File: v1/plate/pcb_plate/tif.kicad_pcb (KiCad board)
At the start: 2 copper layers, 161.7 x 126 mm, 33 parts, among them J2 MJ-4PP-9, SW24 SW_PUSH, SW24B1 SW_PUSH, SW25 SW_PUSH, SW25B1 SW_PUSH, SW26 SW_PUSH, SW26B1 SW_PUSH, U1 ProMicro

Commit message: hole for rotary encoder
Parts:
- removed D23: D, SofleKeyboard-footprint:Diode_SOD123
- removed ROT_ENC: Rotary_Encoder_Switch, SofleKeyboard-footprint:RotaryEncoder_Alps_EC11E-Switch_Vertical_H20mm-keebio_modified
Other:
- outline, holes or cut-outs redrawn
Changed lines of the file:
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@@
   (general
     (thickness 1.6)
-    (drawings 121)
+    (drawings 124)
     (tracks 956)
     (zones 0)
-    (modules 33)
+    (modules 31)
     (nets 54)
   )
@@
       (net 28 "Net-(D24-Pad2)"))
   )
-  (module SofleKeyboard-footprint:RotaryEncoder_Alps_EC11E-Switch_Vertical_H20mm-keebio_modified (layer F.Cu)
-    (at 163.0299 126.2126 180)
-    (descr "Alps rotary encoder, EC12E... with switch, vertical shaft, http://www.alps.com/prod/info/E/HTML/Encoder/Incremental/EC11/EC11E15204A3.html")
-    (tags "rotary encoder")
-    (fp_text reference ROT_ENC (at -0.0127 8.3693) (layer F.SilkS)
-      (effects (font (size 1 1) (thickness 0.15)))
-    )
-    (fp_text value Rotary_Encoder_Switch (at 0 7.9) (layer F.Fab)
-      (effects (font (size 1 1) (thickness 0.15)))
-    )
-    (fp_line (start -0.5 0) (end 0.5 0) (layer B.SilkS) (width 0.12))
-    (fp_line (start 0 -0.5) (end 0 0.5) (layer B.SilkS) (width 0.12))
-    (fp_circle (center 0 0) (end 3 0) (layer B.SilkS) (width 0.12))
-    (fp_line (start 2 -5.9) (end 6.1 -5.9) (layer B.SilkS) (width 0.12))
-    (fp_line (start 6.1 -5.9) (end 6.1 -3.5) (layer B.SilkS) (width 0.12))
-    (fp_line (start 6.1 -1.3) (end 6.1 1.3) (layer B.SilkS) (width 0.12))
-    (fp_line (start 6.1 3.5) (end 6.1 5.9) (layer B.SilkS) (width 0.12))
-    (fp_line (start 6.1 5.9) (end 2 5.9) (layer B.SilkS) (width 0.12))
-    (fp_line (start -2 5.9) (end -6.1 5.9) (layer B.SilkS) (width 0.12))
-    (fp_line (start -6.1 -5.9) (end -6.1 5.9) (layer B.SilkS) (width 0.12))
-    (fp_line (start -2 -5.9) (end -6.1 -5.9) (layer B.SilkS) (width 0.12))
-    (fp_line (start -0.5 0) (end 0.5 0) (layer F.SilkS) (width 0.12))
-    (fp_line (start 0 -0.5) (end 0 0.5) (layer F.SilkS) (width 0.12))
-    (fp_line (start 6.1 3.5) (end 6.1 5.9) (layer F.SilkS) (width 0.12))
-    (fp_line (start 6.1 -1.3) (end 6.1 1.3) (layer F.SilkS) (width 0.12))
-    (fp_line (start 6.1 -5.9) (end 6.1 -3.5) (layer F.SilkS) (width 0.12))
-    (fp_line (start -3 0) (end 3 0) (layer F.Fab) (width 0.12))
-    (fp_line (start 0 -3) (end 0 3) (layer F.Fab) (width 0.12))
-    (fp_line (start -6.1 -5.9) (end -6.1 5.9) (layer F.SilkS) (width 0.12))
-    (fp_line (start -2 -5.9) (end -6.1 -5.9) (layer F.SilkS) (width 0.12))
-    (fp_line (start -2 5.9) (end -6.1 5.9) (layer F.SilkS) (width 0.12))
-    (fp_line (start 6.1 5.9) (end 2 5.9) (layer F.SilkS) (width 0.12))
-    (fp_line (start 2 -5.9) (end 6.1 -5.9) (layer F.SilkS) (width 0.12))
-    (fp_line (start -6 -4.7) (end -5 -5.8) (layer F.Fab) (width 0.12))
-    (fp_line (start -6 5.8) (end -6 -4.7) (layer F.Fab) (width 0.12))
-    (fp_line (start 6 5.8) (end -6 5.8) (layer F.Fab) (width 0.12))
-    (fp_line (start 6 -5.8) (end 6 5.8) (layer F.Fab) (width 0.12))
-    (fp_line (start -5 -5.8) (end 6 -5.8) (layer F.Fab) (width 0.12))
-    (fp_line (start -9 -7.1) (end 8.5 -7.1) (layer F.CrtYd) (width 0.05))
-    (fp_line (start -9 -7.1) (end -9 7.1) (layer F.CrtYd) (width 0.05))
-    (fp_line (start 8.5 7.1) (end 8.5 -7.1) (layer F.CrtYd) (width 0.05))
-    (fp_line (start 8.5 7.1) (end -9 7.1) (layer F.CrtYd) (width 0.05))
-    (fp_circle (center 0 0) (end 3 0) (layer F.SilkS) (width 0.12))
-    (fp_circle (center 0 0) (end 3 0) (layer F.Fab) (width 0.12))
-    (pad S1 thru_hole circle (at 7 2.5 180) (size 2 2) (drill 1) (layers *.Cu *.Mask)
-      (net 46 COL2))
-    (pad S2 thru_hole circle (at 7 -2.5 180) (size 2 2) (drill 1) (layers *.Cu *.Mask)
-      (net 52 SW23B))
-    (pad MP thru_hole rect (at 0 5.6 180) (size 3.2 2) (drill oval 2.8 1.5) (layers *.Cu *.Mask))
-    (pad MP thru_hole rect (at 0 -5.6 180) (size 3.2 2) (drill oval 2.8 1.5) (layers *.Cu *.Mask))
-    (pad B thru_hole circle (at -7.5 2.5 180) (size 2 2) (drill 1) (layers *.Cu *.Mask)
-      (net 40 ENCB))
-    (pad C thru_hole circle (at -7.5 0 180) (size 2 2) (drill 1) (layers *.Cu *.Mask)
-      (net 34 GND))
-    (pad A thru_hole circle (at -7.5 -2.5 180) (size 2 2) (drill 1) (layers *.Cu *.Mask)
-      (net 41 ENCA))
-    (model ${KISYS3DMOD}/Rotary_Encoder.3dshapes/RotaryEncoder_Alps_EC11E-Switch_Vertical_H20mm.wrl
-      (at (xyz 0 0 0))
-      (scale (xyz 1 1 1))
-      (rotate (xyz 0 0 0))
-    )
-  )
   (module footprints:SW_PUSH_6mm (layer F.Cu)
     (at 200.5965 71.7169 270)
@@
     )
   )
-  (module SofleKeyboard-footprint:Diode_SOD123 placed (layer F.Cu)
-    (at 161.0106 128.6891 180)
-    (descr "Diode, DO-41, SOD81, Horizontal, RM 10mm,")
-    (tags "Diode, DO-41, SOD81, Horizontal, RM 10mm, 1N4007, SB140,")
-    (fp_text reference D23 (at 0 1.5) (layer F.SilkS) hide
-      (effects (font (size 1 1) (thickness 0.15)))
-    )
-    (fp_text value D (at 0 -1.2) (layer F.Fab) hide
-      (effects (font (size 1 1) (thickness 0.15)))
-    )
-    (fp_line (start -0.5 -0.7) (end -0.5 0.7) (layer F.SilkS) (width 0.15))
-    (fp_line (start -0.5 0) (end 0.4 -0.7) (layer F.SilkS) (width 0.15))
-    (fp_line (start 0.4 0.7) (end -0.5 0) (layer F.SilkS) (width 0.15))
-    (fp_line (start 0.4 -0.7) (end 0.4 0.7) (layer F.SilkS) (width 0.15))
-    (fp_line (start -0.5 -0.7) (end -0.5 0.7) (layer B.SilkS) (width 0.15))
-    (fp_line (start 0.4 0.7) (end -0.5 0) (layer B.SilkS) (width 0.15))
-    (fp_line (start 0.4 -0.7) (end 0.4 0.7) (layer B.SilkS) (width 0.15))
-    (fp_line (start -0.5 0) (end 0.4 -0.7) (layer B.SilkS) (width 0.15))
-    (pad 2 thru_hole rect (at 1.7 0 180) (size 1.8 1.5) (drill 0.4) (layers *.Cu *.Mask)
-      (net 52 SW23B))
-    (pad 1 thru_hole rect (at -1.7 0 180) (size 1.8 1.5) (drill 0.4) (layers *.Cu *.Mask)
-      (net 27 ROW4))
-    (model ${KISYS3DMOD}/Diode_SMD.3dshapes/D_SOD-123.wrl
-      (offset (xyz 0 0 -1.7))
-      (scale (xyz 1 1 1))
-      (rotate (xyz 180 0 0))
-    )
-  )
+  (gr_line (start 156.6699 132.5226) (end 156.6699 119.9026) (layer Edge.Cuts) (width 0.05))
+  (gr_line (start 169.3899 132.5226) (end 156.6699 132.5226) (layer Edge.Cuts) (width 0.05))
+  (gr_line (start 169.3899 119.9026) (end 169.3899 132.5226) (layer Edge.Cuts) (width 0.05))
+  (gr_line (start 156.6699 119.9026) (end 169.3899 119.9026) (layer Edge.Cuts) (width 0.05))
   (gr_line (start 85.68892 111.775) (end 99.68892 111.775) (layer Edge.Cuts) (width 0.05))
   (gr_line (start 99.68892 111.775) (end 99.68892 97.775) (layer Edge.Cuts) (width 0.05))
@@
   (gr_line (start 210.564542 163.394934) (end 225.6155 154.7114) (layer Edge.Cuts) (width 0.05))
   (gr_line (start 65.024 69.2531) (end 65.024 120.8151) (layer Edge.Cuts) (width 0.05))
-  (gr_circle (center 163.0299 126.2126) (end 153.5938 122.5931) (layer Dwgs.User) (width 0.15))
   (segment (start 80.01 72.39) (end 80.01 73.66) (width 0.25) (layer B.Cu) (net 1))
   (segment (start 78.74 71.12) (end 80.01 72.39) (width 0.25) (layer B.Cu) (net 1))

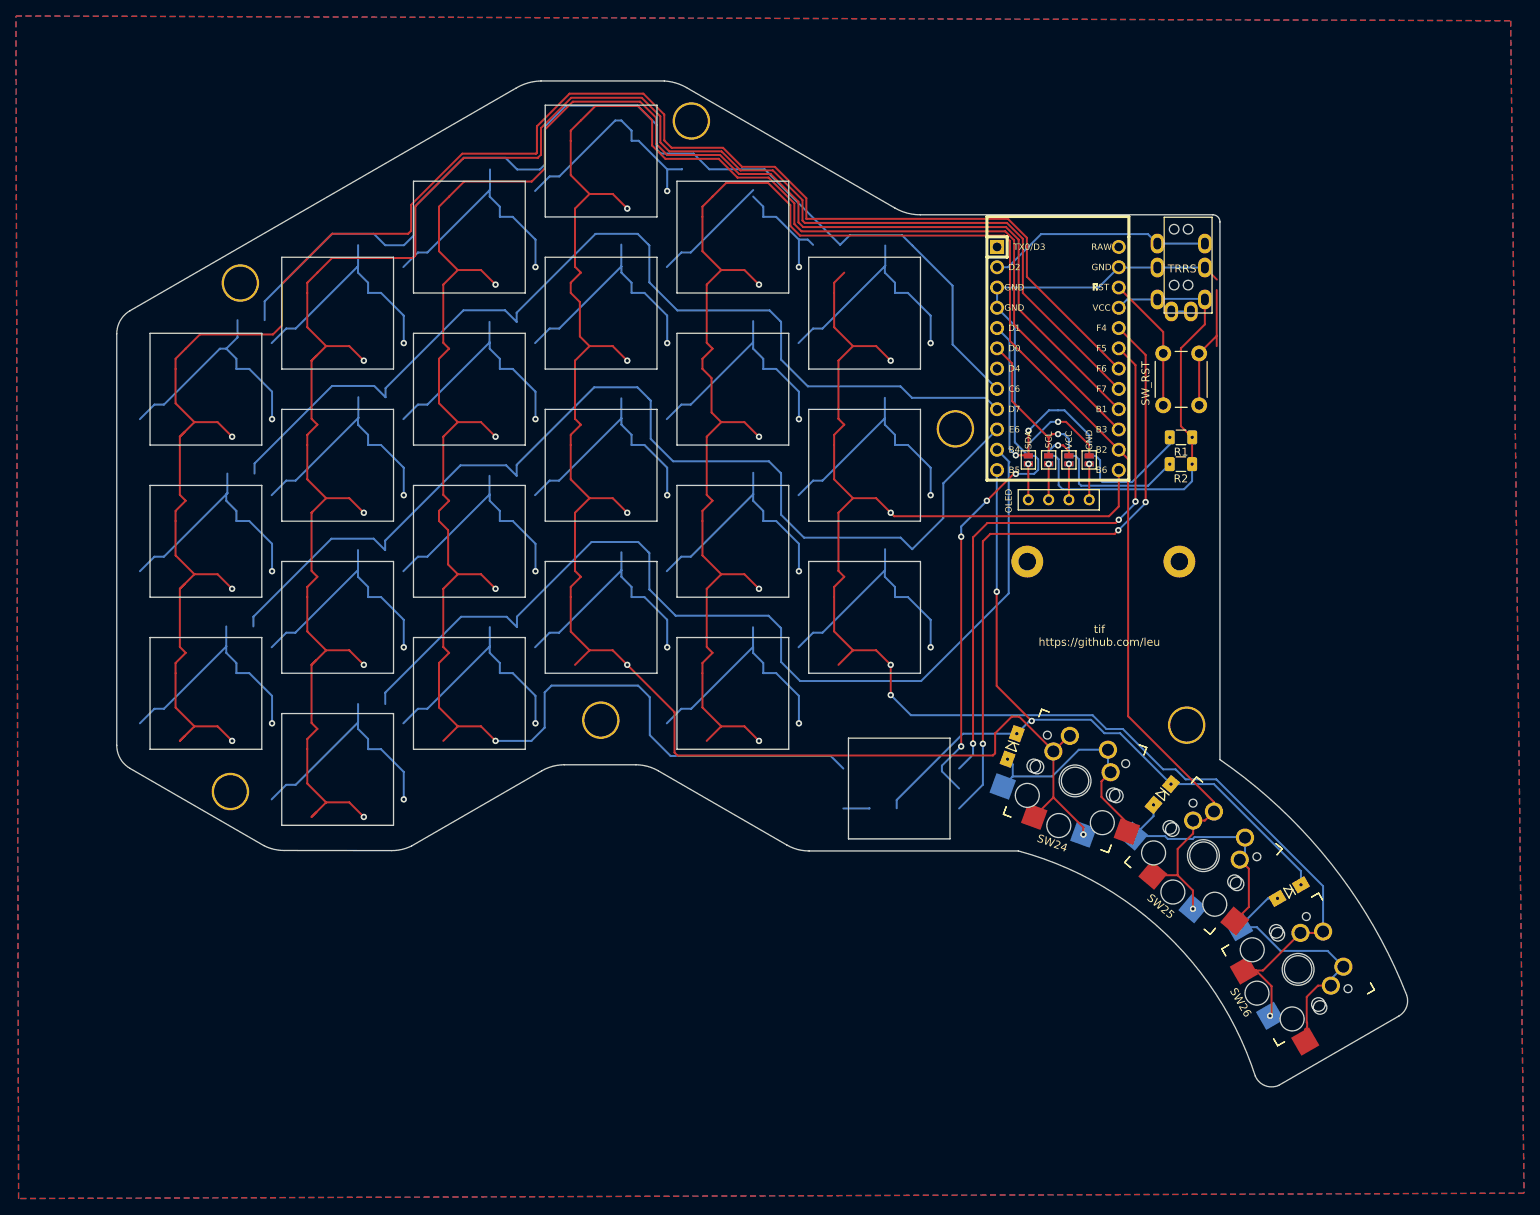
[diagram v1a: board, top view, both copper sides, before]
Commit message: finished top plate switch mounts, switched holes on plate
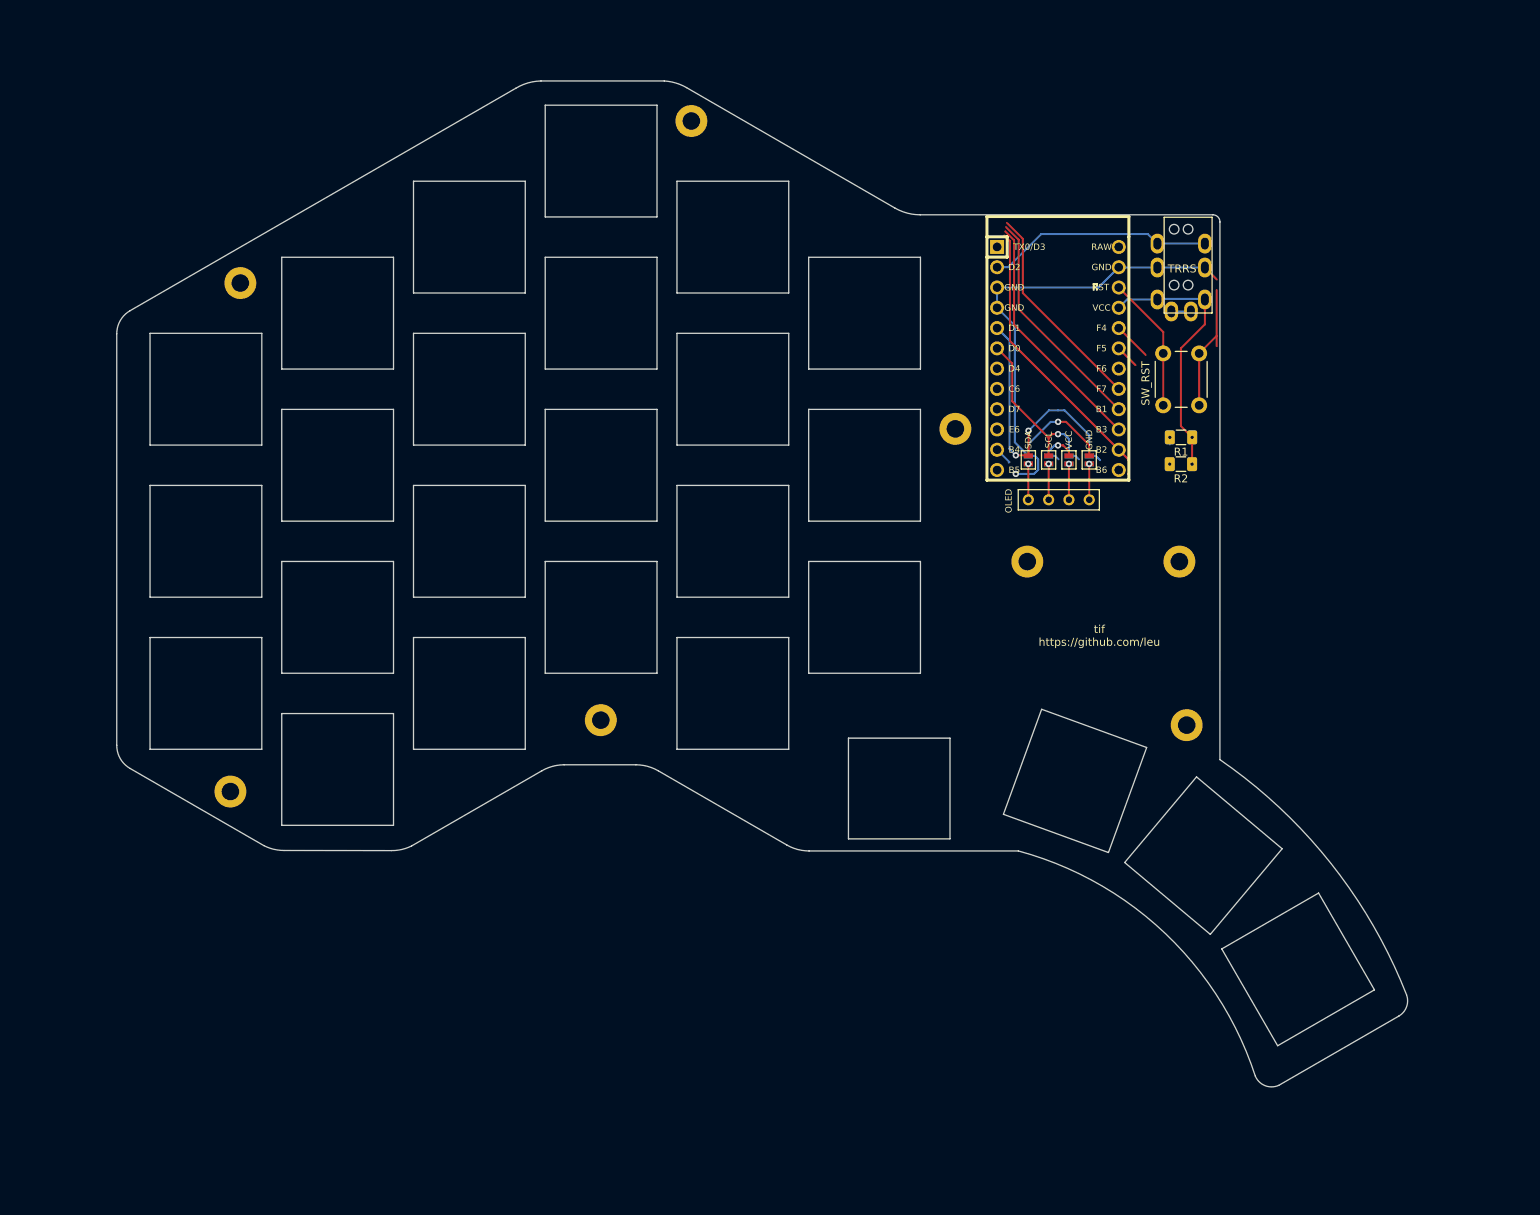
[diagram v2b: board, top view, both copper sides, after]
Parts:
- removed D24, D25, D26: D, SofleKeyboard-footprint:Diode_SOD123
- removed SW24, SW25, SW26: SW_PUSH, keyswitches:MX_reversible
- removed SW24B1, SW25B1, SW26B1: SW_PUSH, keyswitches:PG1350_socket_reversible
- H1, H2, H3, H4, H5, H6: footprint SofleKeyboard-footprint:HOLE_M2_TH -> SofleKeyboard-footprint:M2_HOLE_PCB
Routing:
- net COL3: track 279.2 -> 30.7 mm, vias 5 -> 0
- net COL2: track 272.3 -> 28.7 mm, vias 4 -> 0
- net COL0: track 233.0 -> 0.00 mm, vias 3 -> 0
- net COL1: track 240.3 -> 26.6 mm, vias 4 -> 0
- net COL4: track 243.4 -> 36.4 mm, vias 5 -> 0
- net COL5: track 198.8 -> 0.00 mm, vias 5 -> 0
- net ROW0: track 133.3 -> 0.00 mm
- net ROW2: track 133.1 -> 0.00 mm
- net ROW1: track 124.4 -> 0.00 mm
- net ROW3: track 124.7 -> 2.28 mm
- net ROW4: track 98.9 -> 0.02 mm, vias 2 -> 0
- net ENCA: track 80.4 -> 4.76 mm, vias 3 -> 0
- net ENCB: track 72.1 -> 2.96 mm, vias 3 -> 0
- net GND: track 131.5 -> 87.4 mm, vias 5 -> 2
- net Net-(D26-Pad2): track 33.7 -> 0.00 mm
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- removed copper zone on B.Cu, net GND
- removed copper zone on F.Cu, net GND
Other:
- outline, holes or cut-outs redrawn
